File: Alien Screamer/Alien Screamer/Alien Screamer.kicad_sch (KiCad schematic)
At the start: 61 parts, among them J1 AudioJack2, Q1 2N3904, Q2 2N3904, Q3 Q_NJFET_DSG, SW1 PWR, SW2 LFO_Shaping, SW3 LFO_Shaping, SW4 SYNC, U1 LM324, U2 LM386

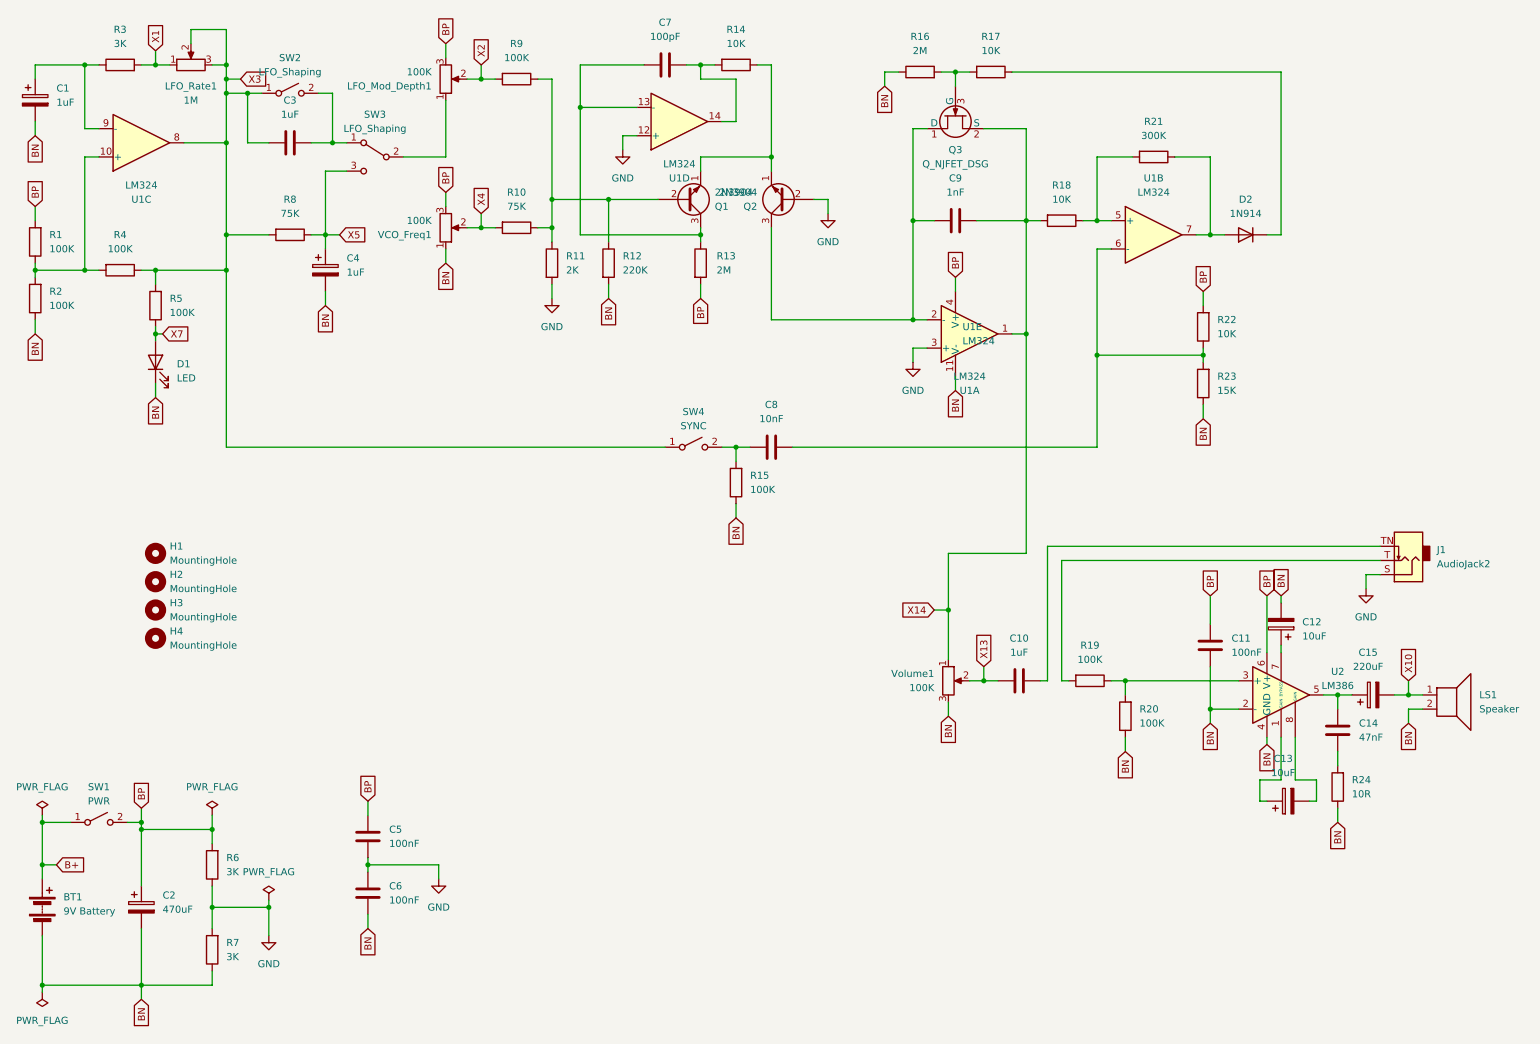
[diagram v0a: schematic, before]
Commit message: Alien Screamer - nicer looking - cap sizes
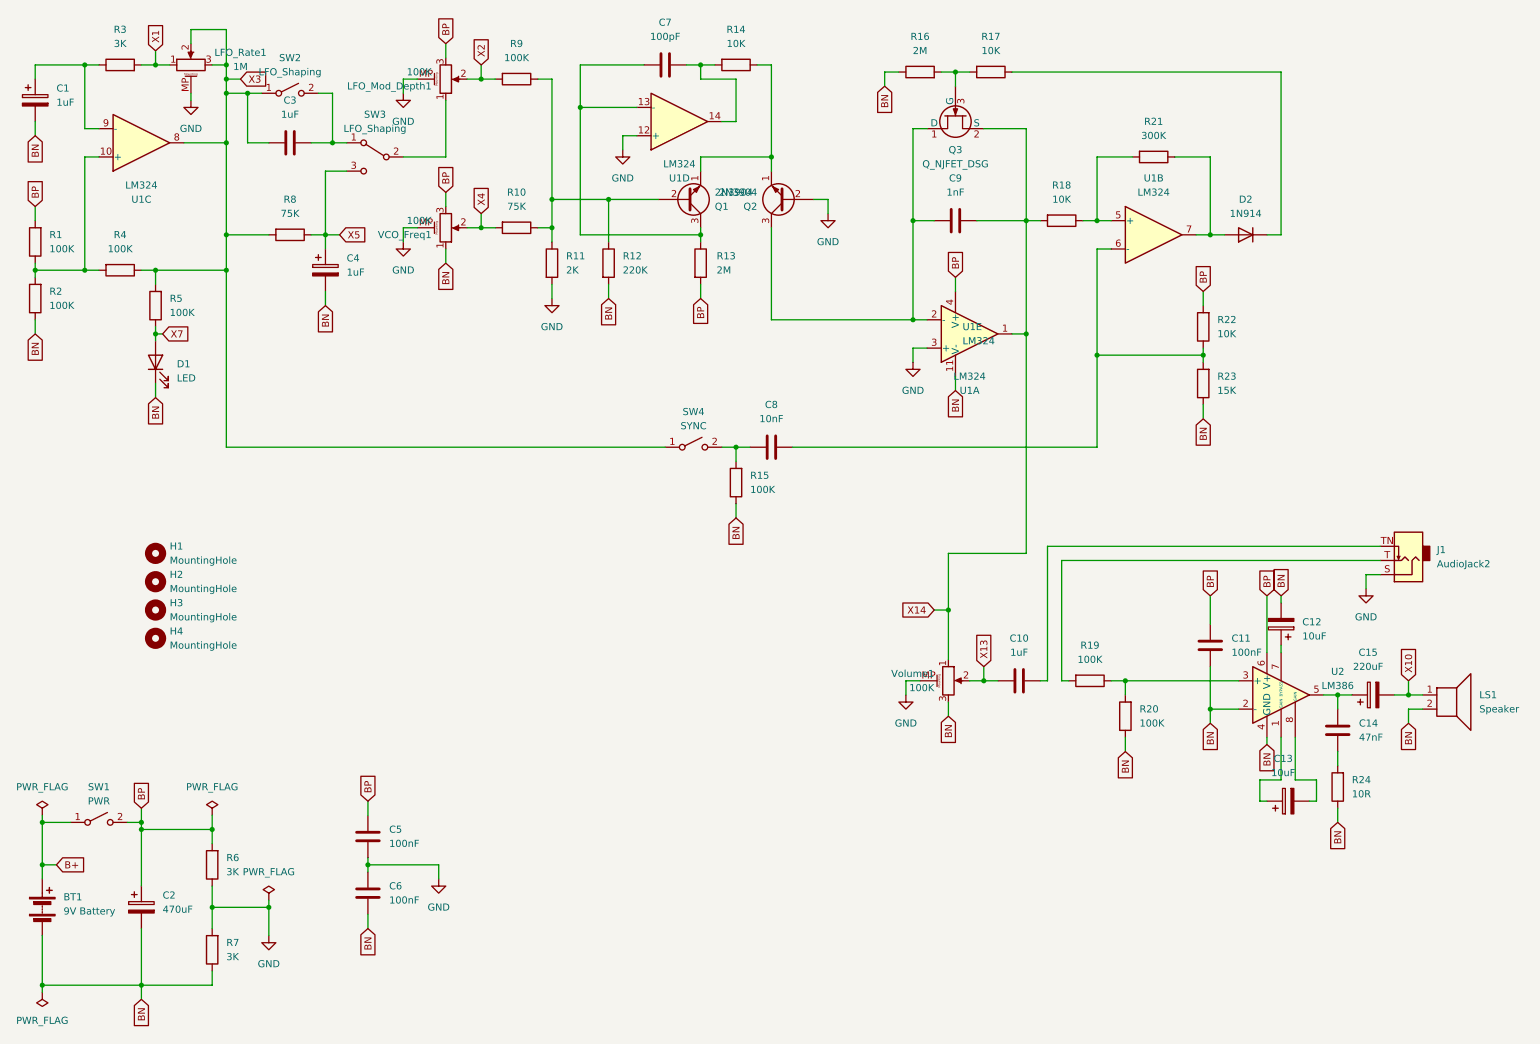
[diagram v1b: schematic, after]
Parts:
- C1, C4: footprint Capacitor_THT:CP_Radial_D4.0mm_P2.00mm -> Capacitor_THT:CP_Radial_D5.0mm_P2.00mm
- C10, C3: footprint Capacitor_THT:C_Radial_D4.0mm_H5.0mm_P1.50mm -> Capacitor_THT:C_Radial_D5.0mm_H5.0mm_P2.00mm
- C12, C13: footprint Capacitor_THT:CP_Radial_D4.0mm_P2.00mm -> Capacitor_THT:CP_Radial_D5.0mm_P2.50mm
- C15, C2: footprint Capacitor_THT:CP_Radial_D4.0mm_P2.00mm -> Capacitor_THT:CP_Radial_D8.0mm_P3.80mm
- LFO_Mod_Depth1, LFO_Rate1, VCO_Freq1, Volume1: symbol Device:R_Potentiometer -> Device:R_Potentiometer_MountingPin
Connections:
- net GND: now also LFO_Mod_Depth1.MP (MountPin), LFO_Rate1.MP (MountPin), VCO_Freq1.MP (MountPin), Volume1.MP (MountPin)
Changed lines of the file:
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@@
+    (stroke (width 0) (type default))
+  )
+  (wire (pts (xy 82.55 24.13) (xy 82.55 26.67))
     (stroke (width 0) (type default))
   )
@@
     (stroke (width 0) (type default))
   )
+  (wire (pts (xy 82.55 50.8) (xy 82.55 53.34))
+    (stroke (width 0) (type default))
+  )
   (wire (pts (xy 240.03 125.73) (xy 240.03 127))
     (stroke (width 0) (type default))
@@
     (stroke (width 0) (type default))
   )
+  (wire (pts (xy 44.45 26.67) (xy 44.45 27.94))
+    (stroke (width 0) (type default))
+  )
   (wire (pts (xy 139.7 31.75) (xy 142.24 31.75))
     (stroke (width 0) (type default))
@@
     (stroke (width 0) (type default))
   )
+  (wire (pts (xy 175.26 132.08) (xy 172.72 132.08))
+    (stroke (width 0) (type default))
+  )
   (wire (pts (xy 44.45 15.24) (xy 44.45 17.78))
     (stroke (width 0) (type default))
@@
     (stroke (width 0) (type default))
   )
+  (wire (pts (xy 85.09 50.8) (xy 82.55 50.8))
+    (stroke (width 0) (type default))
+  )
   (wire (pts (xy 114.3 29.21) (xy 114.3 52.07))
     (stroke (width 0) (type default))
   )
+  (wire (pts (xy 172.72 132.08) (xy 172.72 134.62))
+    (stroke (width 0) (type default))
+  )
   (wire (pts (xy 35.56 21.59) (xy 38.1 21.59))
     (stroke (width 0) (type default))
@@
   )
   (wire (pts (xy 50.8 90.17) (xy 50.8 58.42))
+    (stroke (width 0) (type default))
+  )
+  (wire (pts (xy 85.09 24.13) (xy 82.55 24.13))
     (stroke (width 0) (type default))
   )
@@
     )
   )
-  (symbol (lib_id "Device:R_Potentiometer") (at 180.34 132.08 0) (unit 1)
+  (symbol (lib_id "Device:R_Potentiometer_MountingPin") (at 180.34 132.08 0) (unit 1)
     (in_bom yes) (on_board yes) (dnp no)
     (property "Reference" "Volume1" (at 177.8 130.81 0)
@@
     (pin "2")
     (pin "3")
+    (pin "MP")
     (instances
       (project "Alien Screamer"
@@
       (effects (font (size 1.27 1.27)))
     )
-    (property "Footprint" "Capacitor_THT:CP_Radial_D4.0mm_P2.00mm" (at 245.11 152.7048 0)
+    (property "Footprint" "Capacitor_THT:CP_Radial_D5.0mm_P2.50mm" (at 245.11 152.7048 0)
       (effects (font (size 1.27 1.27)) hide)
     )
@@
       (effects (font (size 1.27 1.27)) (justify left))
     )
-    (property "Footprint" "Capacitor_THT:CP_Radial_D4.0mm_P2.00mm" (at 69.5452 62.23 0)
+    (property "Footprint" "Capacitor_THT:CP_Radial_D5.0mm_P2.00mm" (at 69.5452 62.23 0)
       (effects (font (size 1.27 1.27)) hide)
     )
@@
     )
   )
-  (symbol (lib_id "Device:R_Potentiometer") (at 44.45 21.59 90) (unit 1)
-    (in_bom yes) (on_board yes) (dnp no) (fields_autoplaced)
-    (property "Reference" "LFO_Rate1" (at 44.45 25.4 90)
-      (effects (font (size 1.27 1.27)))
-    )
-    (property "Value" "1M" (at 44.45 27.94 90)
+  (symbol (lib_id "Device:R_Potentiometer_MountingPin") (at 44.45 21.59 90) (unit 1)
+    (in_bom yes) (on_board yes) (dnp no) (fields_autoplaced)
+    (property "Reference" "LFO_Rate1" (at 53.34 19.3741 90)
+      (effects (font (size 1.27 1.27)))
+    )
+    (property "Value" "1M" (at 53.34 21.9141 90)
       (effects (font (size 1.27 1.27)))
     )
@@
     (pin "2")
     (pin "3")
+    (pin "MP")
     (instances
       (project "Alien Screamer"
         (path "/79298690-8ac0-4a54-afff-4fe219b2da43"
           (reference "LFO_Rate1") (unit 1)
+        )
+      )
+    )
+  )
+  (symbol (lib_id "power:GND") (at 82.55 26.67 0) (unit 1)
+    (in_bom yes) (on_board yes) (dnp no) (fields_autoplaced)
+    (property "Reference" "#PWR09" (at 82.55 33.02 0)
+      (effects (font (size 1.27 1.27)) hide)
+    )
+    (property "Value" "GND" (at 82.55 31.75 0)
+      (effects (font (size 1.27 1.27)))
+    )
+    (property "Footprint" "" (at 82.55 26.67 0)
+      (effects (font (size 1.27 1.27)) hide)
+    )
+    (property "Datasheet" "" (at 82.55 26.67 0)
+      (effects (font (size 1.27 1.27)) hide)
+    )
+    (pin "1")
+    (instances
+      (project "Alien Screamer"
+        (path "/79298690-8ac0-4a54-afff-4fe219b2da43"
+          (reference "#PWR09") (unit 1)
         )
       )
@@
       (effects (font (size 1.27 1.27)))
     )
-    (property "Footprint" "Capacitor_THT:CP_Radial_D4.0mm_P2.00mm" (at 260.35 133.6548 0)
+    (property "Footprint" "Capacitor_THT:CP_Radial_D8.0mm_P3.80mm" (at 260.35 133.6548 0)
       (effects (font (size 1.27 1.27)) hide)
     )
@@
     )
   )
-  (symbol (lib_id "Device:R_Potentiometer") (at 90.17 24.13 0) (mirror x) (unit 1)
+  (symbol (lib_id "Device:R_Potentiometer_MountingPin") (at 90.17 24.13 0) (mirror x) (unit 1)
     (in_bom yes) (on_board yes) (dnp no)
     (property "Reference" "LFO_Mod_Depth1" (at 87.63 25.4 0)
@@
     (pin "2")
     (pin "3")
+    (pin "MP")
     (instances
       (project "Alien Screamer"
@@
       (effects (font (size 1.27 1.27)) (justify right))
     )
-    (property "Footprint" "Capacitor_THT:CP_Radial_D4.0mm_P2.00mm" (at 239.0648 118.11 0)
+    (property "Footprint" "Capacitor_THT:CP_Radial_D5.0mm_P2.50mm" (at 239.0648 118.11 0)
       (effects (font (size 1.27 1.27)) hide)
     )
@@
       (effects (font (size 1.27 1.27)))
     )
-    (property "Footprint" "Capacitor_THT:C_Radial_D4.0mm_H5.0mm_P1.50mm" (at 196.85 131.1148 0)
+    (property "Footprint" "Capacitor_THT:C_Radial_D5.0mm_H5.0mm_P2.00mm" (at 196.85 131.1148 0)
       (effects (font (size 1.27 1.27)) hide)
     )
@@
       (effects (font (size 1.27 1.27)))
     )
-    (property "Footprint" "Capacitor_THT:C_Radial_D4.0mm_H5.0mm_P1.50mm" (at 66.04 34.5948 0)
+    (property "Footprint" "Capacitor_THT:C_Radial_D5.0mm_H5.0mm_P2.00mm" (at 66.04 34.5948 0)
       (effects (font (size 1.27 1.27)) hide)
     )
@@
       (effects (font (size 1.27 1.27)) (justify left))
     )
-    (property "Footprint" "Capacitor_THT:CP_Radial_D4.0mm_P2.00mm" (at 17.4752 31.75 0)
+    (property "Footprint" "Capacitor_THT:CP_Radial_D5.0mm_P2.00mm" (at 17.4752 31.75 0)
       (effects (font (size 1.27 1.27)) hide)
     )
@@
     )
   )
+  (symbol (lib_id "power:GND") (at 172.72 134.62 0) (unit 1)
+    (in_bom yes) (on_board yes) (dnp no) (fields_autoplaced)
+    (property "Reference" "#PWR011" (at 172.72 140.97 0)
+      (effects (font (size 1.27 1.27)) hide)
+    )
+    (property "Value" "GND" (at 172.72 139.7 0)
+      (effects (font (size 1.27 1.27)))
+    )
+    (property "Footprint" "" (at 172.72 134.62 0)
+      (effects (font (size 1.27 1.27)) hide)
+    )
+    (property "Datasheet" "" (at 172.72 134.62 0)
+      (effects (font (size 1.27 1.27)) hide)
+    )
+    (pin "1")
+    (instances
+      (project "Alien Screamer"
+        (path "/79298690-8ac0-4a54-afff-4fe219b2da43"
+          (reference "#PWR011") (unit 1)
+        )
+      )
+    )
+  )
   (symbol (lib_id "Device:R") (at 212.09 138.43 180) (unit 1)
     (in_bom yes) (on_board yes) (dnp no) (fields_autoplaced)
@@
     )
   )
+  (symbol (lib_id "power:GND") (at 44.45 27.94 0) (unit 1)
+    (in_bom yes) (on_board yes) (dnp no) (fields_autoplaced)
+    (property "Reference" "#PWR010" (at 44.45 34.29 0)
+      (effects (font (size 1.27 1.27)) hide)
+    )
+    (property "Value" "GND" (at 44.45 33.02 0)
+      (effects (font (size 1.27 1.27)))
+    )
+    (property "Footprint" "" (at 44.45 27.94 0)
+      (effects (font (size 1.27 1.27)) hide)
+    )
+    (property "Datasheet" "" (at 44.45 27.94 0)
+      (effects (font (size 1.27 1.27)) hide)
+    )
+    (pin "1")
+    (instances
+      (project "Alien Screamer"
+        (path "/79298690-8ac0-4a54-afff-4fe219b2da43"
+          (reference "#PWR010") (unit 1)
+        )
+      )
+    )
+  )
   (symbol (lib_id "Device:C_Polarized") (at 35.56 172.72 0) (unit 1)
     (in_bom yes) (on_board yes) (dnp no) (fields_autoplaced)
@@
       (effects (font (size 1.27 1.27)) (justify left))
     )
-    (property "Footprint" "Capacitor_THT:CP_Radial_D4.0mm_P2.00mm" (at 36.5252 176.53 0)
+    (property "Footprint" "Capacitor_THT:CP_Radial_D8.0mm_P3.80mm" (at 36.5252 176.53 0)
       (effects (font (size 1.27 1.27)) hide)
     )
@@
     )
   )
-  (symbol (lib_id "Device:R_Potentiometer") (at 90.17 50.8 0) (mirror x) (unit 1)
+  (symbol (lib_id "Device:R_Potentiometer_MountingPin") (at 90.17 50.8 0) (mirror x) (unit 1)
     (in_bom yes) (on_board yes) (dnp no)
     (property "Reference" "VCO_Freq1" (at 87.63 52.07 0)
@@
     (pin "2")
     (pin "3")
+    (pin "MP")
     (instances
       (project "Alien Screamer"
@@
         )
       )
+    )
+  )
+  (symbol (lib_id "power:GND") (at 82.55 53.34 0) (unit 1)
+    (in_bom yes) (on_board yes) (dnp no) (fields_autoplaced)
+    (property "Reference" "#PWR08" (at 82.55 59.69 0)
+      (effects (font (size 1.27 1.27)) hide)
+    )
+    (property "Value" "GND" (at 82.55 58.42 0)
+      (effects (font (size 1.27 1.27)))
+    )
+    (property "Footprint" "" (at 82.55 53.34 0)
+      (effects (font (size 1.27 1.27)) hide)
+    )
+    (property "Datasheet" "" (at 82.55 53.34 0)
+      (effects (font (size 1.27 1.27)) hide)
+    )
+    (pin "1")
+    (instances
+      (project "Alien Screamer"
+        (path "/79298690-8ac0-4a54-afff-4fe219b2da43"
+          (reference "#PWR08") (unit 1)
+        )
+      )
